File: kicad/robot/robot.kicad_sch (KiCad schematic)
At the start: 46 parts, among them U1 DNP

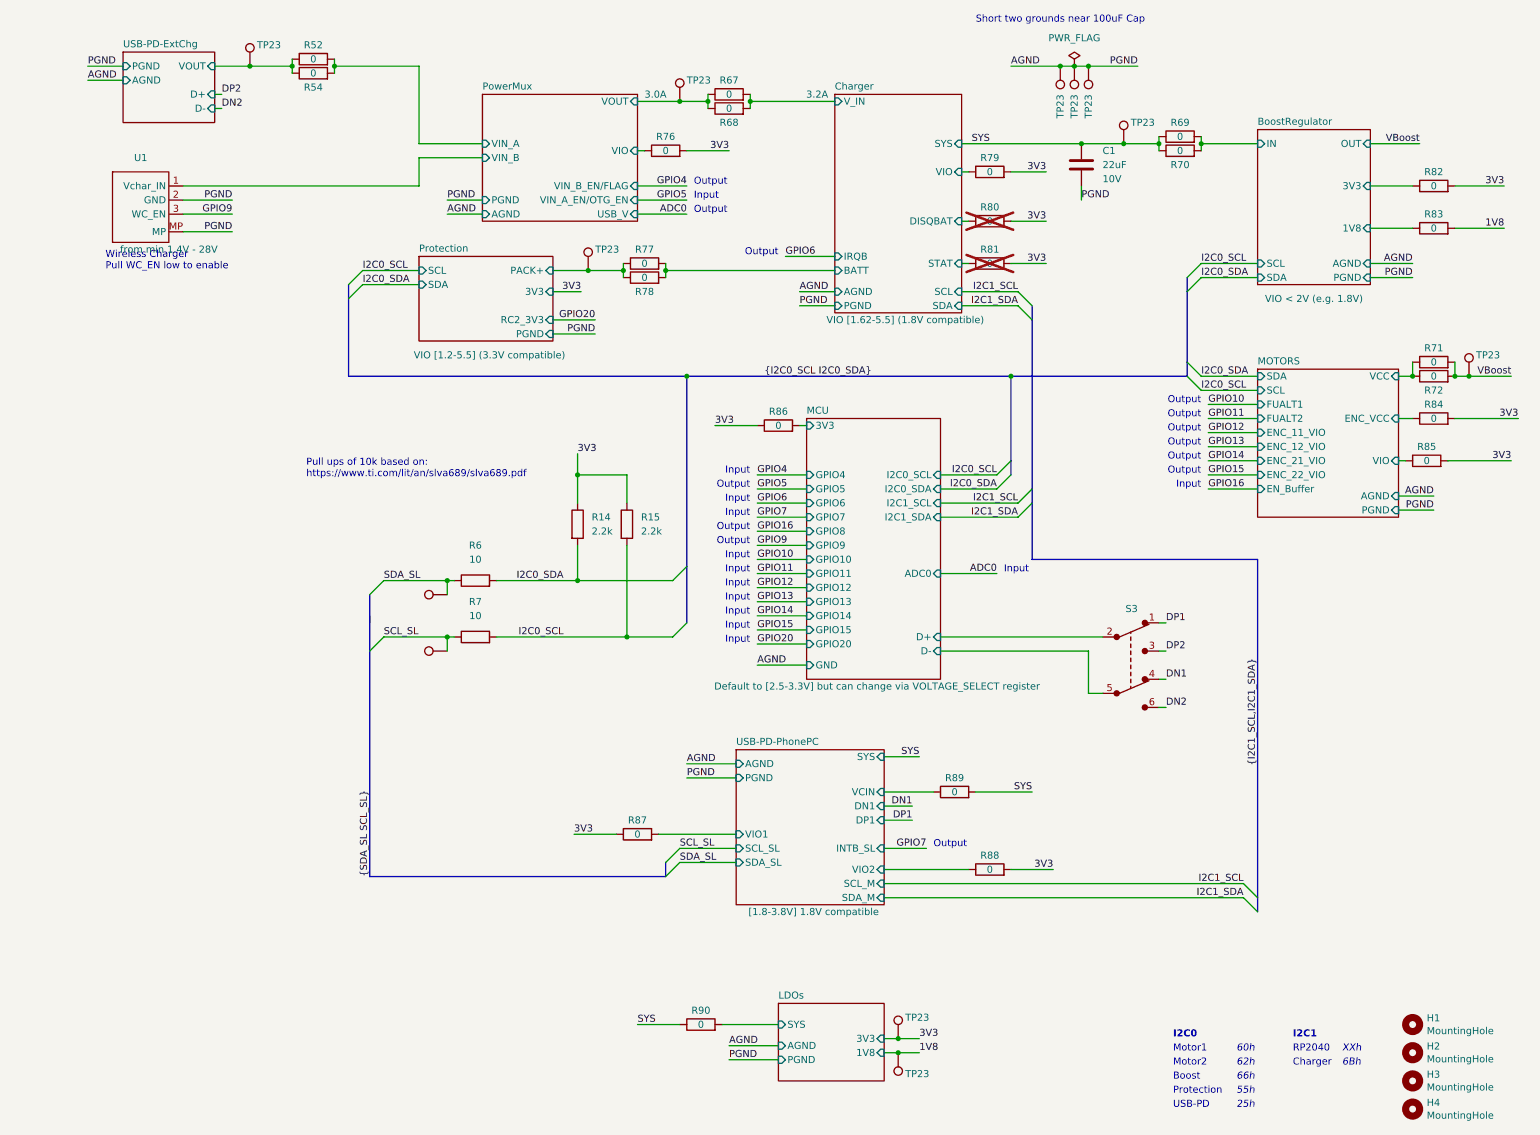
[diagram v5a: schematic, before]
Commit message: Replaced all test points with SMD parts where possible
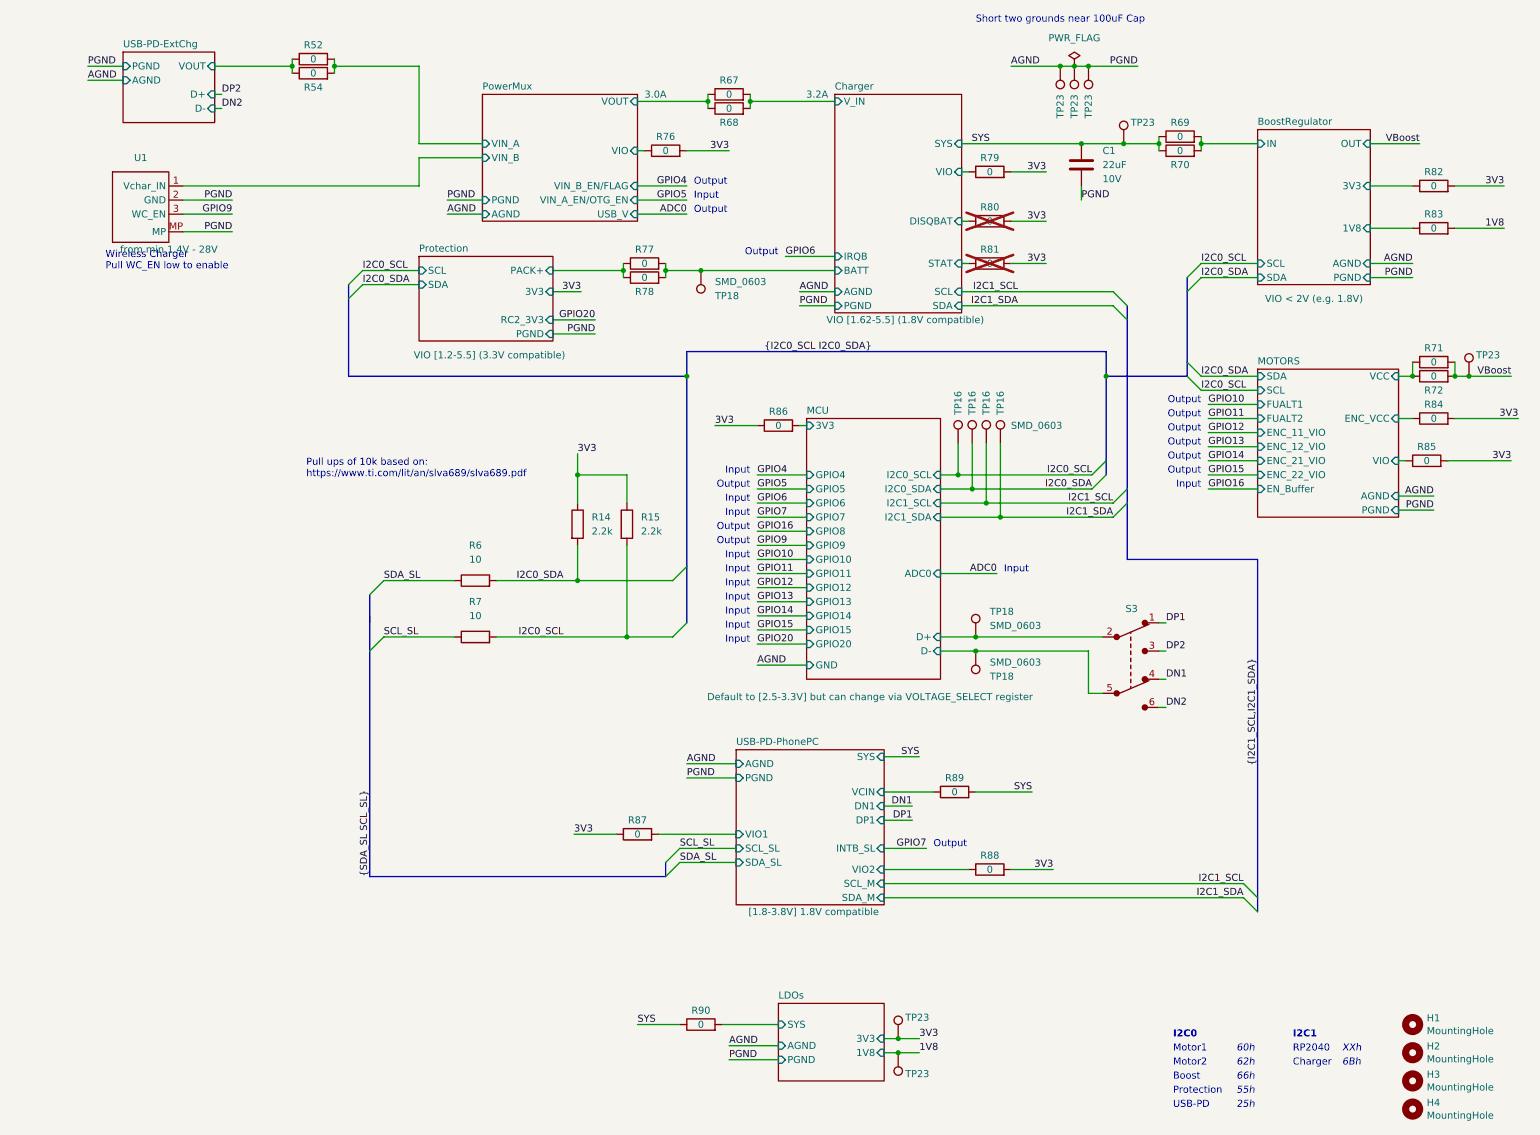
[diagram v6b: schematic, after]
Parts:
- removed TP1, TP2, TP23 (x3): TestPoint, robot:KEYSTONE_5002, symbol robot:TestPoint
- added TP16 (x4), TP18 (x3): SMD_0603, robot:TestPoint_SMD_0603, symbol robot:TestPoint
- R6, R7: footprint robot:R_0402_1005Metric -> robot:R_0603_1608Metric; Manufacturer Yageo -> (none); Part Number RC0402FR-1310RL -> (none)
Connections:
- net Charger/BATT: now also TP18.1
- net I2C0_SCL: now also TP16.1
- net I2C0_SDA: now also TP16.1
- net I2C1_SCL: now also TP16.1
- net I2C1_SDA: now also TP16.1
- net MCU/D+: now also TP18.1
- net MCU/D-: now also TP18.1

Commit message: Adding power flags to side of 0ohm resistors for electrical checks
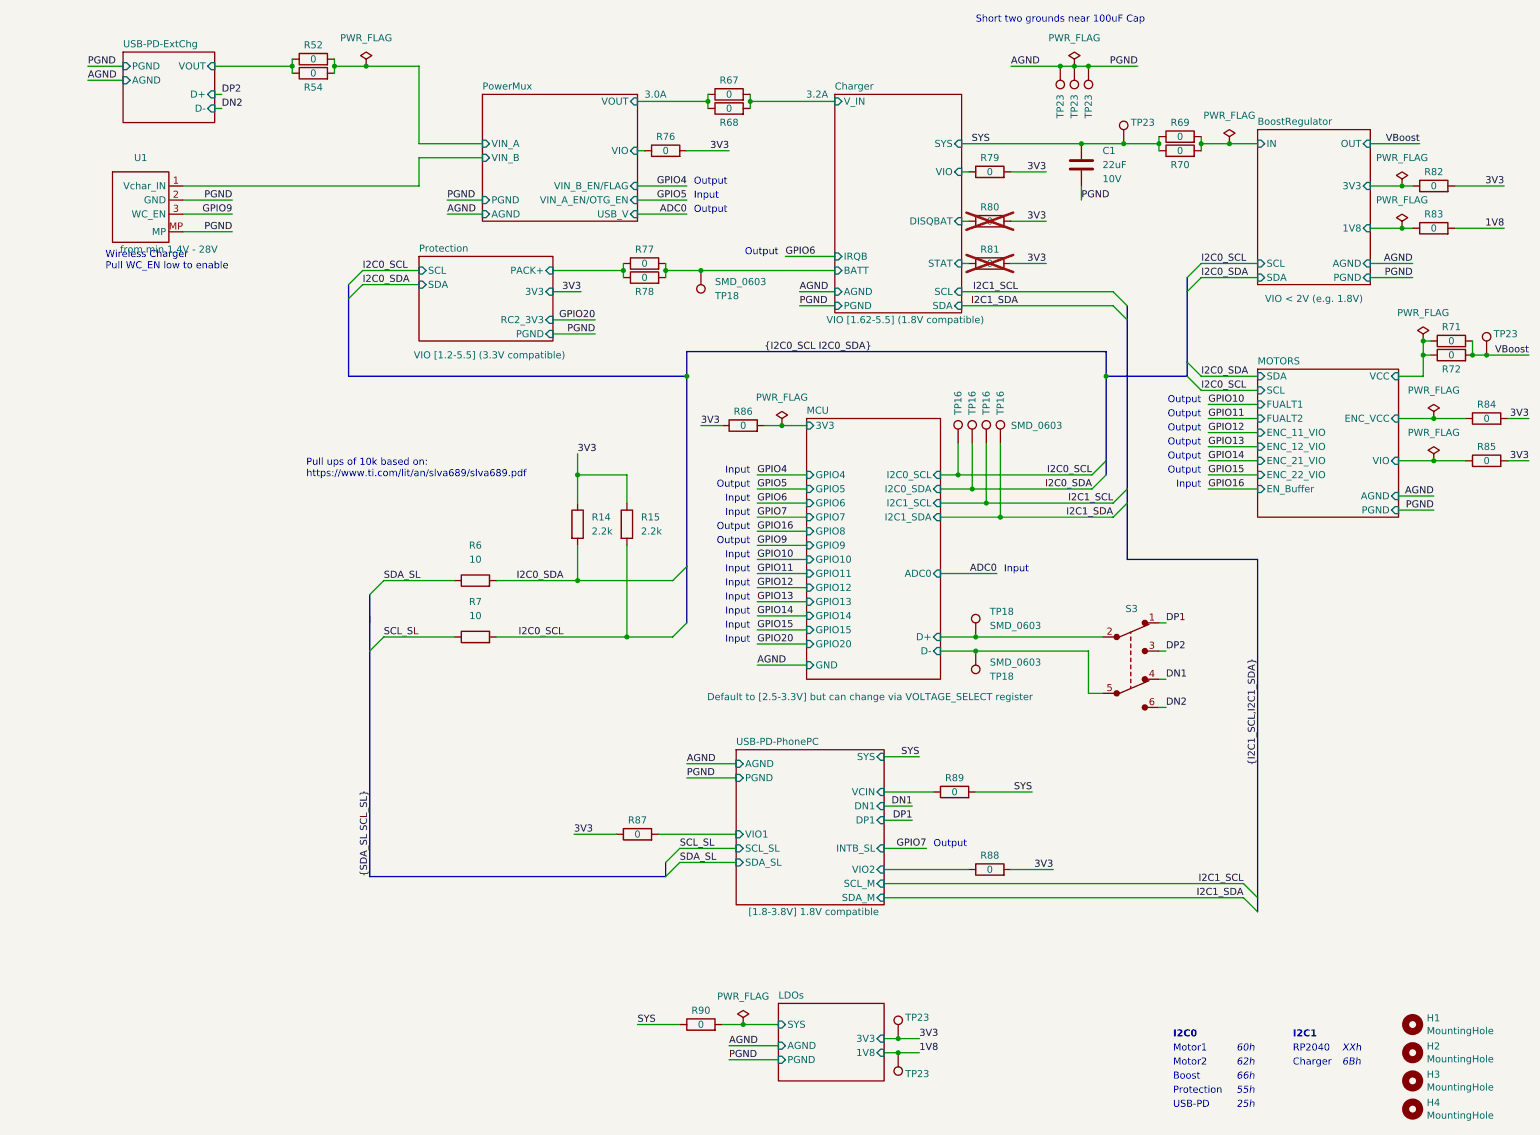
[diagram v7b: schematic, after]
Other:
- moved on the sheet: R71, R72, R84, R85, R86, TP23

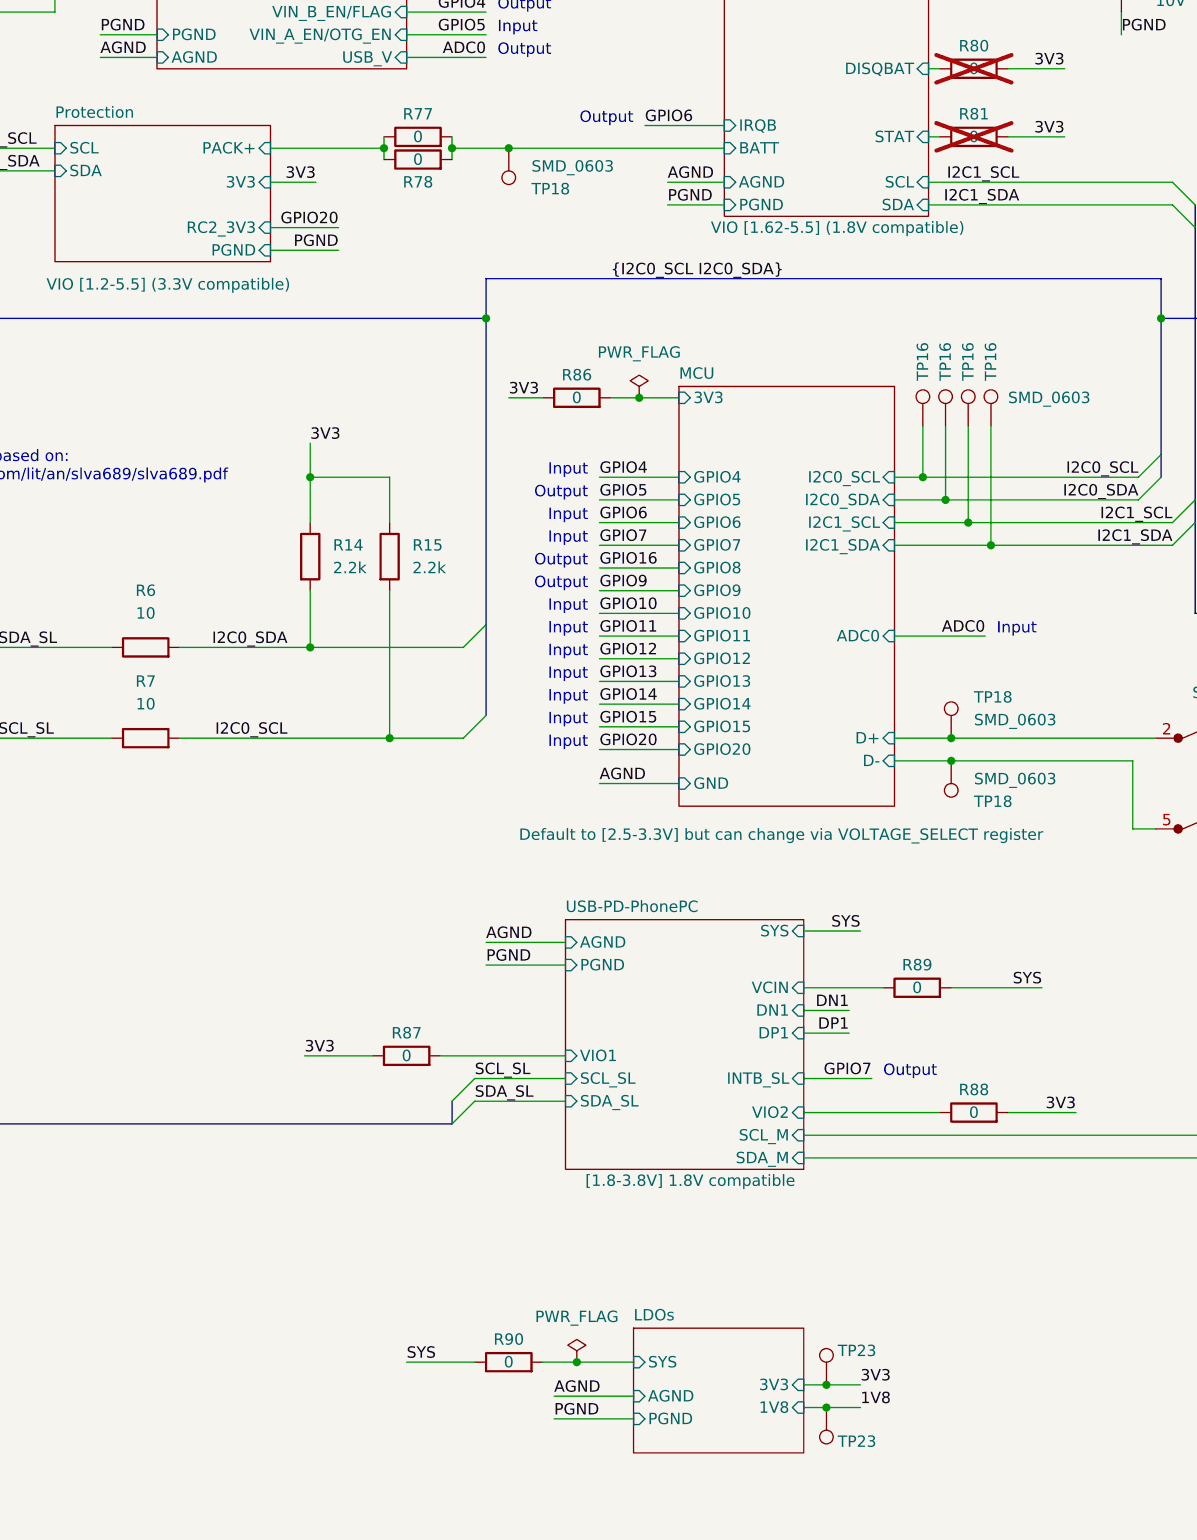
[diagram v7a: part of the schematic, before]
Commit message: Replacing LEDs with side mounted ones, and added an LED driver for the two that don't have a driver
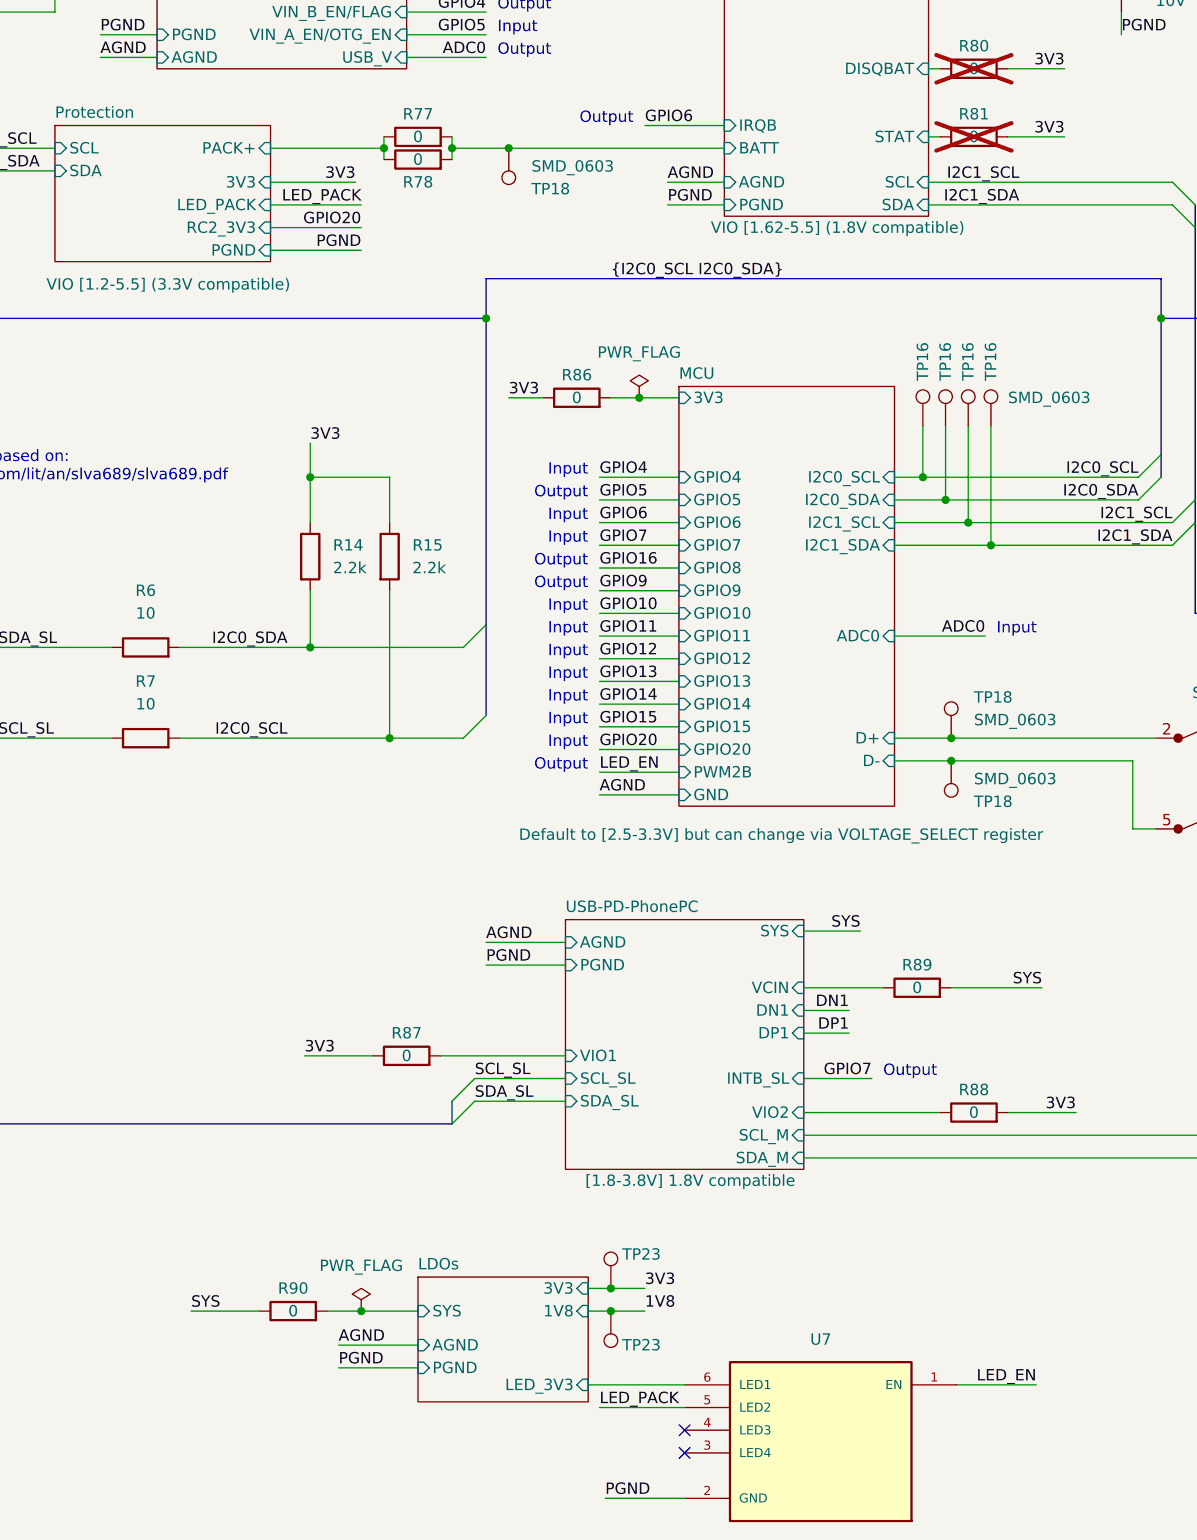
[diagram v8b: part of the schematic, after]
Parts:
- added U7: AP2502KTR-G1, robot:SOT95P280X145-6N, symbol robot:AP2502KTR-G1
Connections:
- net AGND: now also U7.2 (GND)
- new net LDOs/LED_3V3: U7.6 (LED1)
- new net LED_EN: U7.1 (EN)
- new net LED_PACK: U7.5 (LED2)
- no-connect marks 0 -> 2
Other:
- sheet LDOs ports: added LED_3V3; removed none
- sheet MCU ports: added PWM2B; removed none
- sheet Protection ports: added LED_PACK; removed none
- moved on the sheet: R90, TP23
